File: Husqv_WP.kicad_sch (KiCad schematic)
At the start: 10 parts, among them U1 TC4421, U2 TC4422

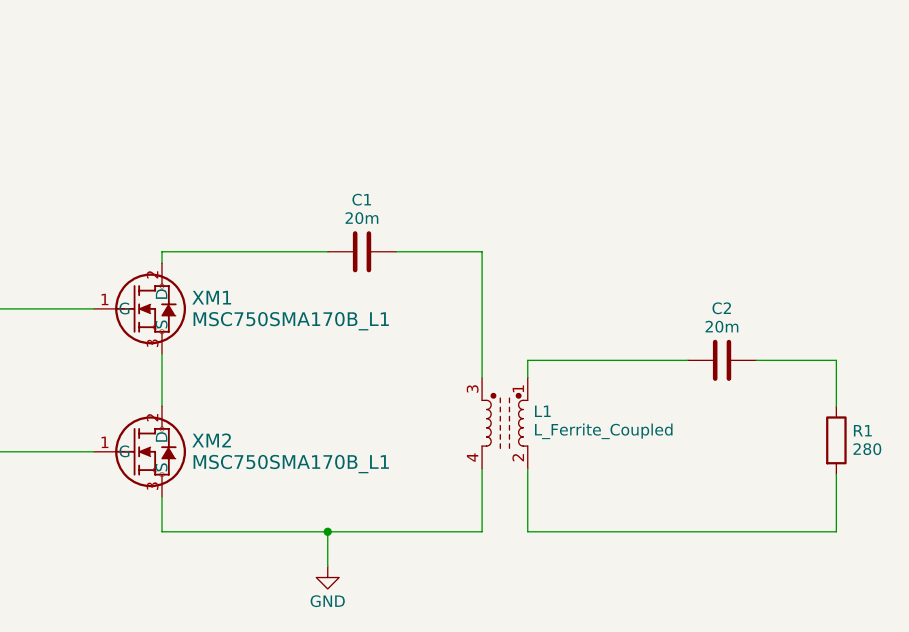
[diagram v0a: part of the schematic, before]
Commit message: Added FREDFETs and th transformer model from https://electronics.stackexchange.com/questions/268176/spice-model-of-coupled-inductor
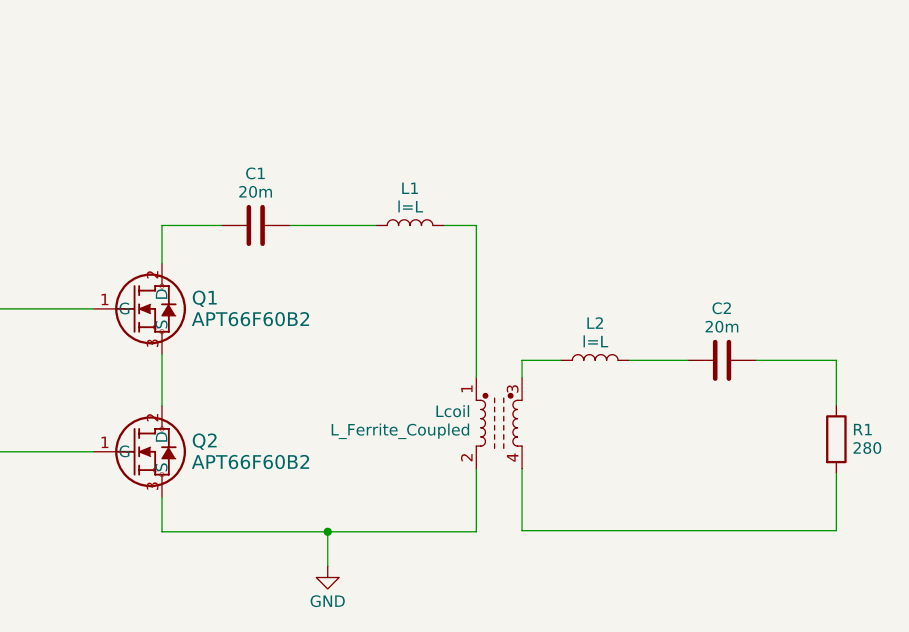
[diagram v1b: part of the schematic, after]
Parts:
- removed L1: L_Ferrite_Coupled, symbol Device:L_Ferrite_Coupled
- removed XM2: MSC750SMA170B_L1, TO-247_MCH, symbol myLibSymbols:MSC750SMA170B
- added L1, L2: ${SIM.PARAMS}, symbol Device:L
- added Lcoil: L_Ferrite_Coupled, symbol Device:L_Ferrite_Coupled
- added Q2: APT66F60B2, Package_TO_SOT_THT:TO-247-3_Horizontal_TabDown, symbol myLibSymbols:MSC750SMA170B
- Q1: renamed from XM1; value MSC750SMA170B_L1 -> APT66F60B2; footprint TO-247_MCH -> Package_TO_SOT_THT:TO-247-3_Horizontal_TabDown
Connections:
- net GND: now also Lcoil.2, Q2.3 (S)
- net at Q1.3 (S): now also Q2.2 (D)
- net at C2.1: now also L2.2
- net at U2.6 (OUTPUT), U2.7 (OUTPUT): now also Q2.1 (G)
- net at R1.2: now also Lcoil.4
- net at C1.2: now also L1.1
- new net: L1.2, Lcoil.1
- new net: L2.1, Lcoil.3
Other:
- moved on the sheet: C1
